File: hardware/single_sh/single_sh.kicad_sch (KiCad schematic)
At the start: 151 parts, among them J1 USB-C, J11 M1+M2, J12 M3+M4, J13 M5+M6, J14 M7+M8, J15 M9+M10, J2 Qwiic, J3 Qwiic, J4 5V IN, J5 LED STRIP, J6 LED PWR, J7 E-STOP, J8 PANEL BTN, Q1 AO3401A, SW1 BTN1, SW2 BTN2, SW3 BOOTSEL, U1 AT8833CQ, U10 AT8833CQ, U11 RP2354B, U12 TPD2E2U06, U13 ME6211C33M5G, U14 74AHCT1G125, U15 74AHCT1G125, U2 AT8833CQ, U3 AT8833CQ, U4 AT8833CQ, U5 AT8833CQ, U6 AT8833CQ, U7 AT8833CQ, U8 AT8833CQ, U9 AT8833CQ, Y1 12MHz

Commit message: single_sh: 0805 sense resistors; JLCPCB fab output
Sense resistors move from 0402 (62.5 mW) to 0805 (125 mW, Yageo
RL0805FR-070R82L, C513694); holding a coil at the current-limit trip is
now 56 % of rating. Driver-cell bottoms re-routed for the larger pads
(BOUT2 between the ISEN pads, BOUT1 under R_B), seven input nets
re-routed, motor labels moved onto the connectors. DRC: 0 unconnected,
no copper violations.

Also adds gen/jlcfab.py and the regenerated JLCPCB Gerbers/BOM/CPL.

Co-Authored-By: Claude Opus 5.5 <noreply@anthropic.com>
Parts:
- R1, R10, R11, R12, R13, R14, R15, R16, R17, R18, R19, R2, R20, R3, R4, R5, R6, R7, R8, R9: footprint Resistor_SMD:R_0402_1005Metric -> Resistor_SMD:R_0805_2012Metric; LCSC C728435 -> C513694; MPN RL0402FR-070R82L -> RL0805FR-070R82L
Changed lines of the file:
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@@
 			)
 		)
-		(property "Footprint" "Resistor_SMD:R_0402_1005Metric"
+		(property "Footprint" "Resistor_SMD:R_0805_2012Metric"
 			(at 116.84 40.64 0)
 			(hide yes)
@@
 			)
 		)
-		(property "LCSC" "C728435"
+		(property "LCSC" "C513694"
 			(at 116.84 40.64 0)
 			(hide yes)
@@
 			)
 		)
-		(property "MPN" "RL0402FR-070R82L"
+		(property "MPN" "RL0805FR-070R82L"
 			(at 116.84 40.64 0)
 			(hide yes)
@@
 			)
 		)
-		(property "Footprint" "Resistor_SMD:R_0402_1005Metric"
+		(property "Footprint" "Resistor_SMD:R_0805_2012Metric"
 			(at 167.64 40.64 0)
 			(hide yes)
@@
 			)
 		)
-		(property "LCSC" "C728435"
+		(property "LCSC" "C513694"
 			(at 167.64 40.64 0)
 			(hide yes)
@@
 			)
 		)
-		(property "MPN" "RL0402FR-070R82L"
+		(property "MPN" "RL0805FR-070R82L"
 			(at 167.64 40.64 0)
 			(hide yes)
@@
 			)
 		)
-		(property "Footprint" "Resistor_SMD:R_0402_1005Metric"
+		(property "Footprint" "Resistor_SMD:R_0805_2012Metric"
 			(at 492.76 40.64 0)
 			(hide yes)
@@
 			)
 		)
-		(property "LCSC" "C728435"
+		(property "LCSC" "C513694"
 			(at 492.76 40.64 0)
 			(hide yes)
@@
 			)
 		)
-		(property "MPN" "RL0402FR-070R82L"
+		(property "MPN" "RL0805FR-070R82L"
 			(at 492.76 40.64 0)
 			(hide yes)
@@
 			)
 		)
-		(property "Footprint" "Resistor_SMD:R_0402_1005Metric"
+		(property "Footprint" "Resistor_SMD:R_0805_2012Metric"
 			(at 543.56 40.64 0)
 			(hide yes)
@@
 			)
 		)
-		(property "LCSC" "C728435"
+		(property "LCSC" "C513694"
 			(at 543.56 40.64 0)
 			(hide yes)
@@
 			)
 		)
-		(property "MPN" "RL0402FR-070R82L"
+		(property "MPN" "RL0805FR-070R82L"
 			(at 543.56 40.64 0)
 			(hide yes)
@@
 			)
 		)
-		(property "Footprint" "Resistor_SMD:R_0402_1005Metric"
+		(property "Footprint" "Resistor_SMD:R_0805_2012Metric"
 			(at 116.84 86.36 0)
 			(hide yes)
@@
 			)
 		)
-		(property "LCSC" "C728435"
+		(property "LCSC" "C513694"
 			(at 116.84 86.36 0)
 			(hide yes)
@@
 			)
 		)
-		(property "MPN" "RL0402FR-070R82L"
+		(property "MPN" "RL0805FR-070R82L"
 			(at 116.84 86.36 0)
 			(hide yes)
@@
 			)
 		)
-		(property "Footprint" "Resistor_SMD:R_0402_1005Metric"
+		(property "Footprint" "Resistor_SMD:R_0805_2012Metric"
 			(at 167.64 86.36 0)
 			(hide yes)
@@
 			)
 		)
-		(property "LCSC" "C728435"
+		(property "LCSC" "C513694"
 			(at 167.64 86.36 0)
 			(hide yes)
@@
 			)
 		)
-		(property "MPN" "RL0402FR-070R82L"
+		(property "MPN" "RL0805FR-070R82L"
 			(at 167.64 86.36 0)
 			(hide yes)
@@
 			)
 		)
-		(property "Footprint" "Resistor_SMD:R_0402_1005Metric"
+		(property "Footprint" "Resistor_SMD:R_0805_2012Metric"
 			(at 492.76 86.36 0)
 			(hide yes)
@@
 			)
 		)
-		(property "LCSC" "C728435"
+		(property "LCSC" "C513694"
 			(at 492.76 86.36 0)
 			(hide yes)
@@
 			)
 		)
-		(property "MPN" "RL0402FR-070R82L"
+		(property "MPN" "RL0805FR-070R82L"
 			(at 492.76 86.36 0)
 			(hide yes)
@@
 			)
 		)
-		(property "Footprint" "Resistor_SMD:R_0402_1005Metric"
+		(property "Footprint" "Resistor_SMD:R_0805_2012Metric"
 			(at 543.56 86.36 0)
 			(hide yes)
@@
 			)
 		)
-		(property "LCSC" "C728435"
+		(property "LCSC" "C513694"
 			(at 543.56 86.36 0)
 			(hide yes)
@@
 			)
 		)
-		(property "MPN" "RL0402FR-070R82L"
+		(property "MPN" "RL0805FR-070R82L"
 			(at 543.56 86.36 0)
 			(hide yes)
@@
 			)
 		)
-		(property "Footprint" "Resistor_SMD:R_0402_1005Metric"
+		(property "Footprint" "Resistor_SMD:R_0805_2012Metric"
 			(at 116.84 129.54 0)
 			(hide yes)
@@
 			)
 		)
-		(property "LCSC" "C728435"
+		(property "LCSC" "C513694"
 			(at 116.84 129.54 0)
 			(hide yes)
@@
 			)
 		)
-		(property "MPN" "RL0402FR-070R82L"
+		(property "MPN" "RL0805FR-070R82L"
 			(at 116.84 129.54 0)
 			(hide yes)
@@
 			)
 		)
-		(property "Footprint" "Resistor_SMD:R_0402_1005Metric"
+		(property "Footprint" "Resistor_SMD:R_0805_2012Metric"
 			(at 167.64 129.54 0)
 			(hide yes)
@@
 			)
 		)
-		(property "LCSC" "C728435"
+		(property "LCSC" "C513694"
 			(at 167.64 129.54 0)
 			(hide yes)
@@
 			)
 		)
-		(property "MPN" "RL0402FR-070R82L"
+		(property "MPN" "RL0805FR-070R82L"
 			(at 167.64 129.54 0)
 			(hide yes)
@@
 			)
 		)
-		(property "Footprint" "Resistor_SMD:R_0402_1005Metric"
+		(property "Footprint" "Resistor_SMD:R_0805_2012Metric"
 			(at 492.76 129.54 0)
 			(hide yes)
@@
 			)
 		)
-		(property "LCSC" "C728435"
+		(property "LCSC" "C513694"
 			(at 492.76 129.54 0)
 			(hide yes)
@@
 			)
 		)
-		(property "MPN" "RL0402FR-070R82L"
+		(property "MPN" "RL0805FR-070R82L"
 			(at 492.76 129.54 0)
 			(hide yes)
@@
 			)
 		)
-		(property "Footprint" "Resistor_SMD:R_0402_1005Metric"
+		(property "Footprint" "Resistor_SMD:R_0805_2012Metric"
 			(at 543.56 129.54 0)
 			(hide yes)
@@
 			)
 		)
-		(property "LCSC" "C728435"
+		(property "LCSC" "C513694"
 			(at 543.56 129.54 0)
 			(hide yes)
@@
 			)
 		)
-		(property "MPN" "RL0402FR-070R82L"
+		(property "MPN" "RL0805FR-070R82L"
 			(at 543.56 129.54 0)
 			(hide yes)
@@
 			)
 		)
-		(property "Footprint" "Resistor_SMD:R_0402_1005Metric"
+		(property "Footprint" "Resistor_SMD:R_0805_2012Metric"
 			(at 116.84 175.26 0)
 			(hide yes)
@@
 			)
 		)
-		(property "LCSC" "C728435"
+		(property "LCSC" "C513694"
 			(at 116.84 175.26 0)
 			(hide yes)
@@
 			)
 		)
-		(property "MPN" "RL0402FR-070R82L"
+		(property "MPN" "RL0805FR-070R82L"
 			(at 116.84 175.26 0)
 			(hide yes)
@@
 			)
 		)
-		(property "Footprint" "Resistor_SMD:R_0402_1005Metric"
+		(property "Footprint" "Resistor_SMD:R_0805_2012Metric"
 			(at 167.64 175.26 0)
 			(hide yes)
@@
 			)
 		)
-		(property "LCSC" "C728435"
+		(property "LCSC" "C513694"
 			(at 167.64 175.26 0)
 			(hide yes)
@@
 			)
 		)
-		(property "MPN" "RL0402FR-070R82L"
+		(property "MPN" "RL0805FR-070R82L"
 			(at 167.64 175.26 0)
 			(hide yes)
@@
 			)
 		)
-		(property "Footprint" "Resistor_SMD:R_0402_1005Metric"
+		(property "Footprint" "Resistor_SMD:R_0805_2012Metric"
 			(at 492.76 175.26 0)
 			(hide yes)
@@
 			)
 		)
-		(property "LCSC" "C728435"
+		(property "LCSC" "C513694"
 			(at 492.76 175.26 0)
 			(hide yes)
@@
 			)
 		)
-		(property "MPN" "RL0402FR-070R82L"
+		(property "MPN" "RL0805FR-070R82L"
 			(at 492.76 175.26 0)
 			(hide yes)
@@
 			)
 		)
-		(property "Footprint" "Resistor_SMD:R_0402_1005Metric"
+		(property "Footprint" "Resistor_SMD:R_0805_2012Metric"
 			(at 543.56 175.26 0)
 			(hide yes)
@@
 			)
 		)
-		(property "LCSC" "C728435"
+		(property "LCSC" "C513694"
 			(at 543.56 175.26 0)
 			(hide yes)
@@
 			)
 		)
-		(property "MPN" "RL0402FR-070R82L"
+		(property "MPN" "RL0805FR-070R82L"
 			(at 543.56 175.26 0)
 			(hide yes)
@@
 			)
 		)
-		(property "Footprint" "Resistor_SMD:R_0402_1005Metric"
+		(property "Footprint" "Resistor_SMD:R_0805_2012Metric"
 			(at 116.84 220.98 0)
 			(hide yes)
@@
 			)
 		)
-		(property "LCSC" "C728435"
+		(property "LCSC" "C513694"
 			(at 116.84 220.98 0)
 			(hide yes)
@@
 			)
 		)
-		(property "MPN" "RL0402FR-070R82L"
+		(property "MPN" "RL0805FR-070R82L"
 			(at 116.84 220.98 0)
 			(hide yes)
@@
 			)
 		)
-		(property "Footprint" "Resistor_SMD:R_0402_1005Metric"
+		(property "Footprint" "Resistor_SMD:R_0805_2012Metric"
 			(at 167.64 220.98 0)
 			(hide yes)
@@
 			)
 		)
-		(property "LCSC" "C728435"
+		(property "LCSC" "C513694"
 			(at 167.64 220.98 0)
 			(hide yes)
@@
 			)
 		)
-		(property "MPN" "RL0402FR-070R82L"
+		(property "MPN" "RL0805FR-070R82L"
 			(at 167.64 220.98 0)
 			(hide yes)
@@
 			)
 		)
-		(property "Footprint" "Resistor_SMD:R_0402_1005Metric"
+		(property "Footprint" "Resistor_SMD:R_0805_2012Metric"
 			(at 492.76 220.98 0)
 			(hide yes)
@@
 			)
 		)
-		(property "LCSC" "C728435"
+		(property "LCSC" "C513694"
 			(at 492.76 220.98 0)
 			(hide yes)
@@
 			)
 		)
-		(property "MPN" "RL0402FR-070R82L"
+		(property "MPN" "RL0805FR-070R82L"
 			(at 492.76 220.98 0)
 			(hide yes)
@@
 			)
 		)
-		(property "Footprint" "Resistor_SMD:R_0402_1005Metric"
+		(property "Footprint" "Resistor_SMD:R_0805_2012Metric"
 			(at 543.56 220.98 0)
 			(hide yes)
@@
 			)
 		)
-		(property "LCSC" "C728435"
+		(property "LCSC" "C513694"
 			(at 543.56 220.98 0)
 			(hide yes)
@@
 			)
 		)
-		(property "MPN" "RL0402FR-070R82L"
+		(property "MPN" "RL0805FR-070R82L"
 			(at 543.56 220.98 0)
 			(hide yes)

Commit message: single_sh: wired multi-sheet schematic
Replace the label-on-every-pin single_sh schematic with a presentable
hierarchical drawing: overview, power and USB, MCU, motor drivers,
connectors and UI (A3 sheets). Parts are wired, rails use power symbols,
inter-sheet signals use global labels, each block is framed with design
notes from the README.

- gen/schdraw.py draws wires/labels/power symbols and traces the drawing
  the way KiCad does; the build fails unless every pin is on the net
  build.py gave it. gen/single_sh_sch.py holds the layout.
- AT8833CQ gets a project symbol (lib/stack.kicad_sym, DRV8833RTY pin
  numbers) arranged so each driver cell draws without crossings.
- Same circuit: KiCad netlist has identical pin groupings, refs, values
  and footprints; BOM export unchanged; ERC 0.
- PCB re-linked to the new symbol paths and net names (/GND -> GND,
  locals -> /<sheet>/<name>); netclass patterns follow. Only path and net
  lines change. DRC unchanged (23 silk/courtyard warnings), 0 unconnected,
  0 parity issues. Fab outputs are exported without net names, so
  jlcpcb/ stays valid.

Co-Authored-By: Claude Opus 5.5 <noreply@anthropic.com>
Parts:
- removed C1, C10, C13, C16, C19, C22, C25, C28, C4, C53, C55, C59, C7: 1u, Capacitor_SMD:C_0402_1005Metric, symbol Device:C
- removed C11, C14, C17, C2, C20, C23, C26, C29, C34, C35, C36, C37, C38, C39, C40, C41, C42, C43, C45, C46, C47, C5, C54, C56, C57, C58, C60, C8: 100n, Capacitor_SMD:C_0402_1005Metric, symbol Device:C
- removed C12, C15, C18, C21, C24, C27, C3, C30, C6, C9: 2.2u, Capacitor_SMD:C_0402_1005Metric, symbol Device:C
- removed C31, C32, C33, C52, C61: 10u, Capacitor_SMD:C_0805_2012Metric, symbol Device:C
- removed C44, C48, C49: 4.7u, Capacitor_SMD:C_0402_1005Metric, symbol Device:C
- removed C50, C51: 15p, Capacitor_SMD:C_0402_1005Metric, symbol Device:C
- removed D1, D3: SS54, Diode_SMD:D_SMA, symbol Device:D_Schottky
- removed D2: XL-2020RGBC-WS2812B, LED_SMD:LED_WS2812B-2020_PLCC4_2.0x2.0mm, symbol LED:WS2812B-2020
- removed F1, F2: 1.5A hold, Fuse:Fuse_1812_4532Metric, symbol Device:Polyfuse
- removed J1: USB-C, Connector_USB:USB_C_Receptacle_HRO_TYPE-C-31-M-12, symbol Connector:USB_C_Receptacle_USB2.0_16P
- removed J11: M1+M2, Connector_JST:JST_SH_BM08B-SRSS-TB_1x08-1MP_P1.00mm_Vertical, symbol Connector_Generic:Conn_01x08
- removed J12: M3+M4, Connector_JST:JST_SH_BM08B-SRSS-TB_1x08-1MP_P1.00mm_Vertical, symbol Connector_Generic:Conn_01x08
- removed J13: M5+M6, Connector_JST:JST_SH_BM08B-SRSS-TB_1x08-1MP_P1.00mm_Vertical, symbol Connector_Generic:Conn_01x08
- removed J14: M7+M8, Connector_JST:JST_SH_BM08B-SRSS-TB_1x08-1MP_P1.00mm_Vertical, symbol Connector_Generic:Conn_01x08
- removed J15: M9+M10, Connector_JST:JST_SH_BM08B-SRSS-TB_1x08-1MP_P1.00mm_Vertical, symbol Connector_Generic:Conn_01x08
- removed J2, J3: Qwiic, Connector_JST:JST_SH_BM04B-SRSS-TB_1x04-1MP_P1.00mm_Vertical, symbol Connector_Generic:Conn_01x04
- removed J4: 5V IN, Connector_JST:JST_PH_B2B-PH-K_1x02_P2.00mm_Vertical, symbol Connector_Generic:Conn_01x02
- removed J5: LED STRIP, Connector_JST:JST_XH_B3B-XH-A_1x03_P2.50mm_Vertical, symbol Connector_Generic:Conn_01x03
- removed J6: LED PWR, Connector_JST:JST_PH_B2B-PH-K_1x02_P2.00mm_Vertical, symbol Connector_Generic:Conn_01x02
- removed J7: E-STOP, Connector_JST:JST_PH_B2B-PH-K_1x02_P2.00mm_Vertical, symbol Connector_Generic:Conn_01x02
- removed J8: PANEL BTN, Connector_JST:JST_PH_B3B-PH-K_1x03_P2.00mm_Vertical, symbol Connector_Generic:Conn_01x03
- removed JP1: QWIIC_SUPPLY, Jumper:SolderJumper-2_P1.3mm_Open_RoundedPad1.0x1.5mm, symbol Jumper:SolderJumper_2_Open
- removed JP2: I2C_PU, Jumper:SolderJumper-2_P1.3mm_Bridged_RoundedPad1.0x1.5mm, symbol Jumper:SolderJumper_2_Bridged
- removed JP3: STRIP_SHARED, Jumper:SolderJumper-2_P1.3mm_Bridged_RoundedPad1.0x1.5mm, symbol Jumper:SolderJumper_2_Bridged
- removed JP4: NO_ESTOP, Jumper:SolderJumper-2_P1.3mm_Bridged_RoundedPad1.0x1.5mm, symbol Jumper:SolderJumper_2_Bridged
- removed L1: 3.3u, Inductor_SMD:L_Cenker_CKCS201610, symbol Device:L
- removed Q1: AO3401A, Package_TO_SOT_SMD:SOT-23, symbol Transistor_FET:AO3401A
- removed R1, R10, R11, R12, R13, R14, R15, R16, R17, R18, R19, R2, R20, R3, R4, R5, R6, R7, R8, R9: 0.82, Resistor_SMD:R_0805_2012Metric, symbol Device:R
- removed R21: 47k, Resistor_SMD:R_0402_1005Metric, symbol Device:R
- removed R22: 39k 1%, Resistor_SMD:R_0402_1005Metric, symbol Device:R
- removed R23, R33, R34, R37, R40: 10k 1%, Resistor_SMD:R_0402_1005Metric, symbol Device:R
- removed R24, R38: 33, Resistor_SMD:R_0402_1005Metric, symbol Device:R
- removed R25, R36: 1k, Resistor_SMD:R_0402_1005Metric, symbol Device:R
- removed R26, R27: 27, Resistor_SMD:R_0402_1005Metric, symbol Device:R
- removed R28, R29: 5.1k, Resistor_SMD:R_0402_1005Metric, symbol Device:R
- removed R30: 100k, Resistor_SMD:R_0402_1005Metric, symbol Device:R
- removed R31, R32, R42: 4.7k, Resistor_SMD:R_0402_1005Metric, symbol Device:R
- removed R35, R41: 3.3k 1%, Resistor_SMD:R_0402_1005Metric, symbol Device:R
- removed R39: 20k 1%, Resistor_SMD:R_0402_1005Metric, symbol Device:R
- removed SW1: BTN1, Button_Switch_SMD:SW_SPST_TS-1088-xR020, symbol Switch:SW_Push
- removed SW2: BTN2, Button_Switch_SMD:SW_SPST_TS-1088-xR020, symbol Switch:SW_Push
- removed SW3: BOOTSEL, Button_Switch_SMD:SW_SPST_TS-1088-xR020, symbol Switch:SW_Push
- removed TP1: SWCLK, TestPoint:TestPoint_Pad_D1.0mm, symbol Connector:TestPoint
- removed TP2: SWDIO, TestPoint:TestPoint_Pad_D1.0mm, symbol Connector:TestPoint
- removed TP3: RUN, TestPoint:TestPoint_Pad_D1.0mm, symbol Connector:TestPoint
- removed TP4: GND, TestPoint:TestPoint_Pad_D1.0mm, symbol Connector:TestPoint
- removed TP5: +3V3, TestPoint:TestPoint_Pad_D1.0mm, symbol Connector:TestPoint
- removed U1, U10, U2, U3, U4, U5, U6, U7, U8, U9: AT8833CQ, Package_DFN_QFN:QFN-16-1EP_4x4mm_P0.65mm_EP2.1x2.1mm, symbol Driver_Motor:DRV8833RTY
- removed U11: RP2354B, Package_DFN_QFN:QFN-80-1EP_10x10mm_P0.4mm_EP3.4x3.4mm, symbol MCU_RaspberryPi:RP2354B
- removed U12: TPD2E2U06, Package_TO_SOT_SMD:SOT-553, symbol Power_Protection:TPD2E2U06DRL
- removed U13: ME6211C33M5G, Package_TO_SOT_SMD:SOT-23-5, symbol Regulator_Linear:ME6211C33M5
- removed U14, U15: 74AHCT1G125, Package_TO_SOT_SMD:SOT-23-5, symbol 74xGxx:74AHCT1G125
- removed Y1: 12MHz, Crystal:Crystal_SMD_3225-4Pin_3.2x2.5mm, symbol Device:Crystal_GND24
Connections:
- no-connect marks 10 -> 0
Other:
- added sheet Connectors and UI (io.kicad_sch)
- added sheet MCU (mcu.kicad_sch)
- added sheet Motor drivers (drivers.kicad_sch)
- added sheet Power (power.kicad_sch)
- note added: "+3V3, V5 CC1, CC2 USB D+ / D- VMOT_SENSE"
- note added: "10x AT8833CQ dual H-bridge 0.82 ohm current-limit sense nSLEEP pull-up, V5 bulk nFAULT onto LADDER"
- note added: "122 x 20 mm, 4 layers (F.Cu parts and signals, In1 GND, In2 V5 with a 3V3 island, B.Cu signals), 1.6 mm. All parts on top. Along the board: USB-C and power path | drivers M4-M1 | MCU | drivers M10-M5 | LED strip. Motor plugs along one long edge (J12 J11 | J15 J14 J13); Qwiic, buttons, e-stop, 5 V in and LED power along the other. Same circuit as the controller / driver / io_sh stack with the boar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"
- note added: "5x JST-SH 8P motor plugs Qwiic x2, status LED, LED strip buttons, e-stop, panel ladder board ID"
- note added: "Board"
- note added: "Controller, universal driver and io_sh connector boards on one 122 x 20 mm, 4-layer PCB. Click a sheet to open it."
- note added: "LADDER (buttons, e-stop, panel, driver nFAULT), BOARD_ID, SDA / SCL, LED_DIN"
- note added: "M1-M10 AIN1/2, BIN1/2 (GPIO0-39)"
- note added: "M1-M10 AOUT1/2, BOUT1/2"
- note added: "RP2350 stepper controller - single board, dual 8 mm micro steppers (single_sh)"
- note added: "RP2354B, 2 MB flash in package core regulator, 12 MHz crystal supply decoupling BOOTSEL, SWD pads"
- note added: "USB-C receptacle, ESD, CC sense PTC, Schottky, soft-start P-FET 3.3 V LDO external 5 V input V5 sense divider"
- company: (none) -> RP2350 stepper controller
- title: Stepper controller - single board, dual 8 mm micro steppers (JST-SH 8P) -> Single board (single_sh) - overview

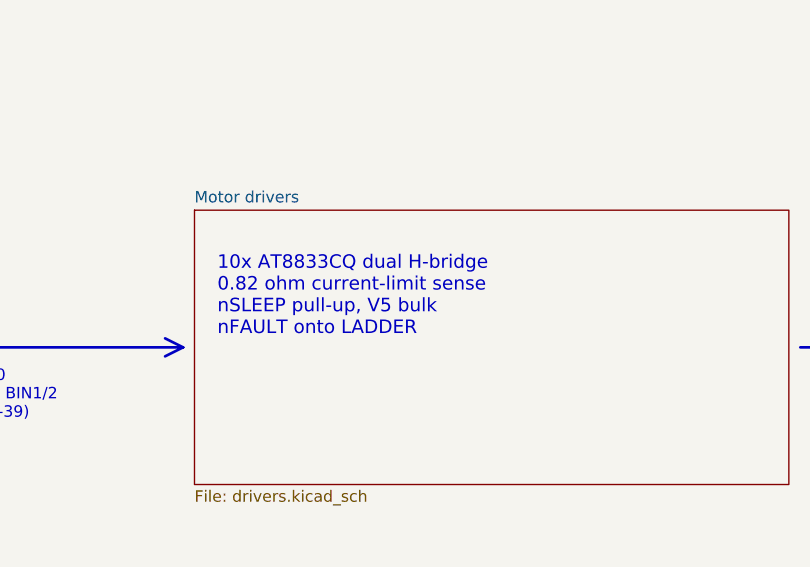
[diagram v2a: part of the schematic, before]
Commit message: single_sh_proto: all-0603 basic-parts prototype board, as ordered
150 x 30 mm 4-layer board, fully routed (0.52/0.3 vias, 45-degree traces,
centred pad entries, no vias in pads), JLCDFM clean. Corrected nested
dual-motor connector pinout, bring-up test points, back-silk squid art.
L1 substituted (C411344); status LED D2 is the 5050 WS2812B (C2843785),
left off the Economic PCBA order for hand soldering.

Generator updates for the proto board (build.py, pcbgen.py, jlcfab.py,
single_sh_sch.py, add_testpoints.py, squid_silk.py) and regenerated
outputs for the other boards.

Ordered from JLCPCB 2026-10-11: 5 boards, Economic PCBA.

Co-Authored-By: Claude Opus 5.5 <noreply@anthropic.com>
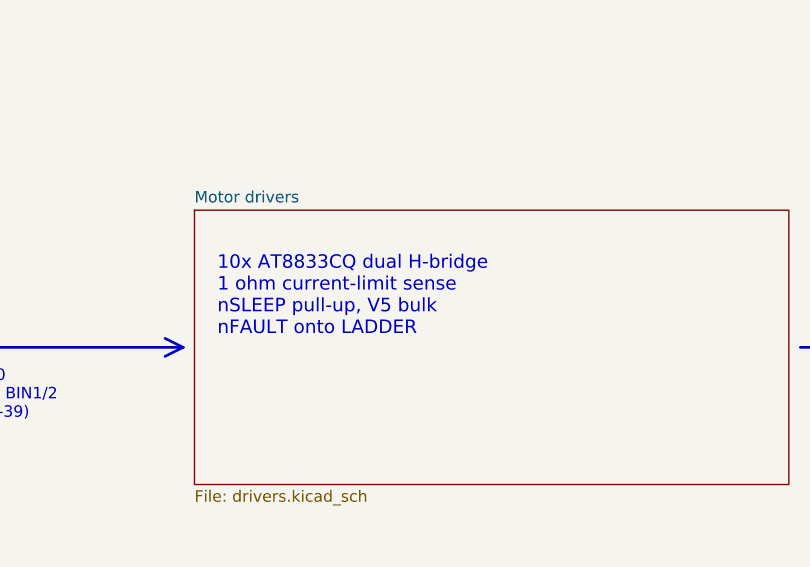
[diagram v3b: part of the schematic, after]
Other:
- note added: "10x AT8833CQ dual H-bridge 1 ohm current-limit sense nSLEEP pull-up, V5 bulk nFAULT onto LADDER"
- note removed: "10x AT8833CQ dual H-bridge 0.82 ohm current-limit sense nSLEEP pull-up, V5 bulk nFAULT onto LADDER"
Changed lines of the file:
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@@
 		)
 	)
-	(text "10x AT8833CQ dual H-bridge\n0.82 ohm current-limit sense\nnSLEEP pull-up, V5 bulk\nnFAULT onto LADDER"
+	(text "10x AT8833CQ dual H-bridge\n1 ohm current-limit sense\nnSLEEP pull-up, V5 bulk\nnFAULT onto LADDER"
 		(exclude_from_sim no)
 		(at 220.98 68.58 0)
